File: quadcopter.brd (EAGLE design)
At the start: 178 x 178 mm, 66 parts, among them J1 ISP, SW1 PUSHBUTTON_SMD-VERTICAL-1, U2 ATMEGA128RFA1

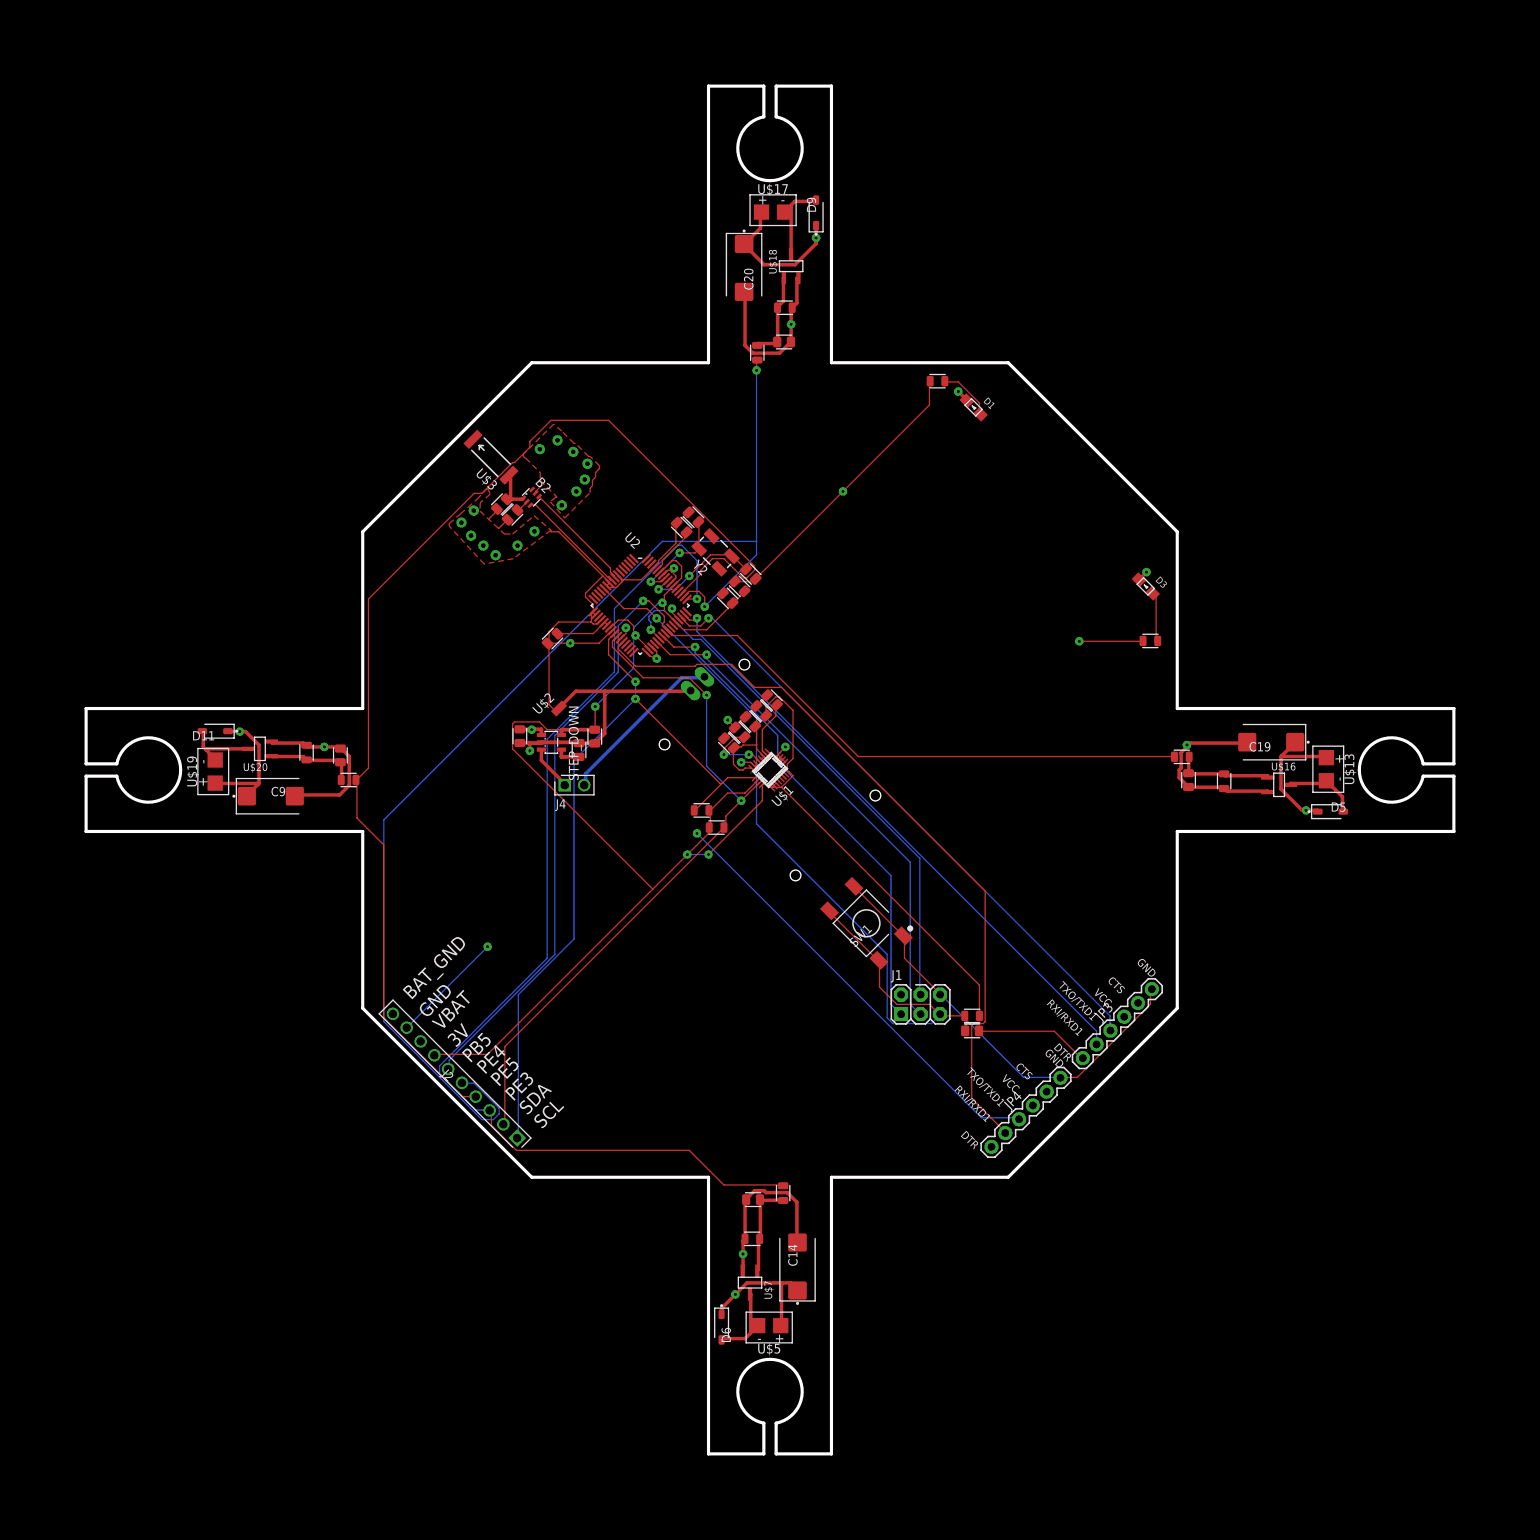
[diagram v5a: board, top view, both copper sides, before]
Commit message: bigger mosfet pads, no vias leading to oscillator, cap 28 and 13 (?) go to gnd instead of bat_gnd, made antenna better
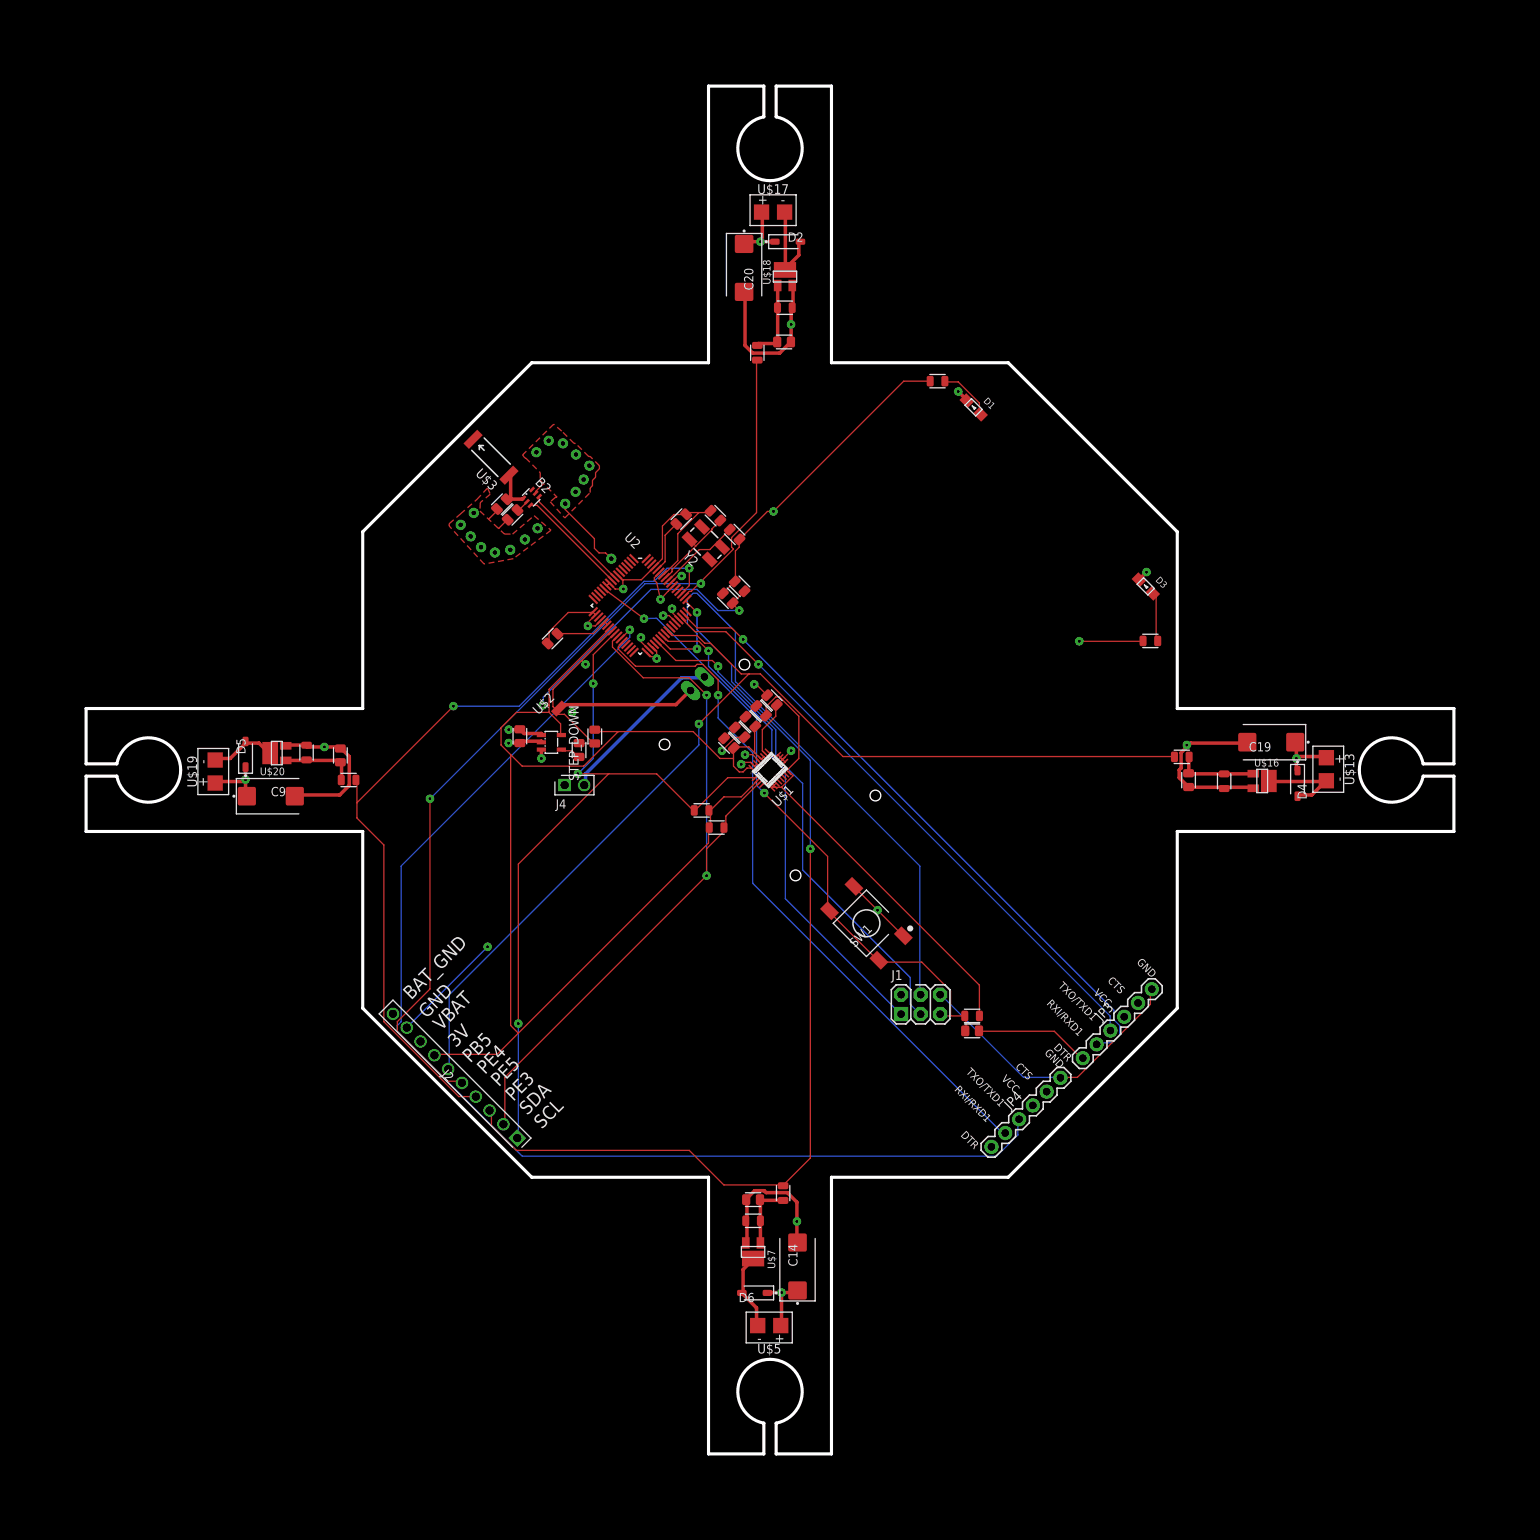
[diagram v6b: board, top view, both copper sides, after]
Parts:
- removed D11, D9: 20V-500MA, quadparts_prebuilt:SOD3716X135_HS
- added D2, D4: (no value), quadparts_prebuilt:SOD3716X135_HS
- D5, D6: value 20V-500MA -> (none)
- moved D5 141.4 mm to (-68.2, 2.05), turned to 90 degrees
- moved D6 6.19 mm to (-2.00, -68.0), turned to 180 degrees
- moved C1 5.56 mm to (-4.60, 30.6)
- moved U$7 4.02 mm to (-2.20, -62.7)
- moved C2 2.86 mm to (-7.10, 33.1)
- moved R10 2.35 mm to (-2.20, -58.7)
- moved U$20 2.27 mm to (-64.2, 2.20)
- moved U$16 2.26 mm to (64.0, -1.43)
- moved Y2 1.73 mm to (-8.34, 29.5)
- moved U$18 1.57 mm to (1.95, 64.2)
- moved C6 1.10 mm to (-11.6, 32.6), turned to 45 degrees
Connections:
- net BAT_GND: no longer C13.2, C28.2
- net FLYBACK: now also D4.A; no longer D5.A
- net FLYBACK1: now also D2.A; no longer D9.A
- net FLYBACK5: now also D5.A; no longer D11.A
- net GND: now also C13.2, C28.2
- net VBAT: now also D2.C, D4.C; no longer D11.C, D9.C
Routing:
- net RX1: track 89.7 -> 157.3 mm, vias 2 -> 1
- net VBAT: track 87.4 -> 41.0 mm, vias 7 -> 8
- net PE5: track 154.8 -> 108.9 mm, vias 0 -> 2
- net 3V: track 244.3 -> 287.6 mm
- net PE4: track 156.7 -> 125.4 mm
- net RESET: track 108.1 -> 84.6 mm, vias 1 -> 2
- net BAT_GND: track 128.8 -> 113.1 mm, vias 5 -> 6
- net PE3: track 143.0 -> 127.8 mm, vias 1 -> 2
- net PB5: track 150.1 -> 140.4 mm
- net MOSI: track 70.2 -> 78.2 mm
- net SDA: track 90.6 -> 98.5 mm
- net TX1: track 97.0 -> 90.8 mm, vias 0 -> 1
- net GND: track 216.0 -> 221.8 mm, vias 24 -> 30
- net TXD1: track 79.1 -> 84.3 mm
- net N$4: track 15.8 -> 11.7 mm, vias 2 -> 0
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
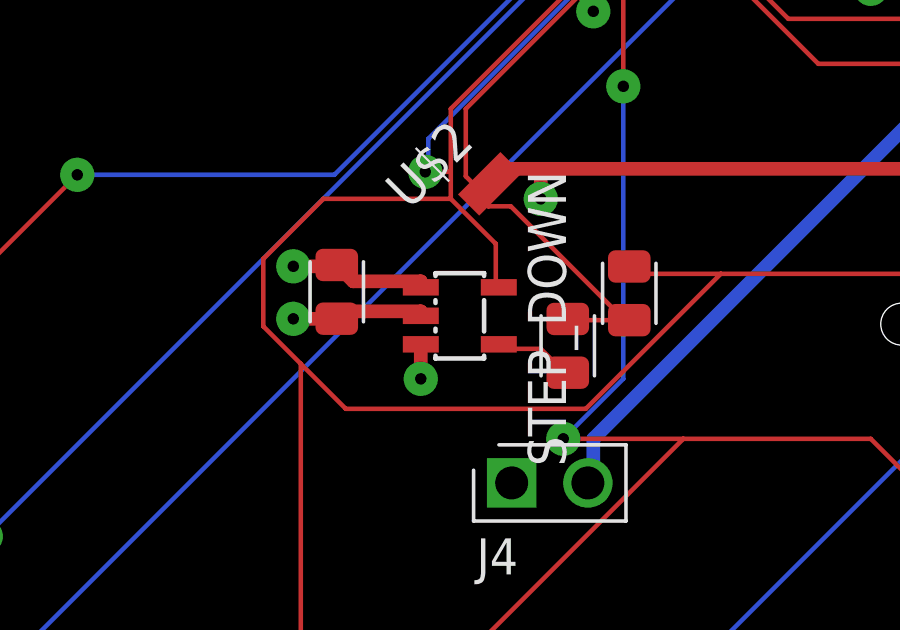
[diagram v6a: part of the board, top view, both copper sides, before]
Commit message: changed most gnds on regulator to gnd instead of bat_gnd
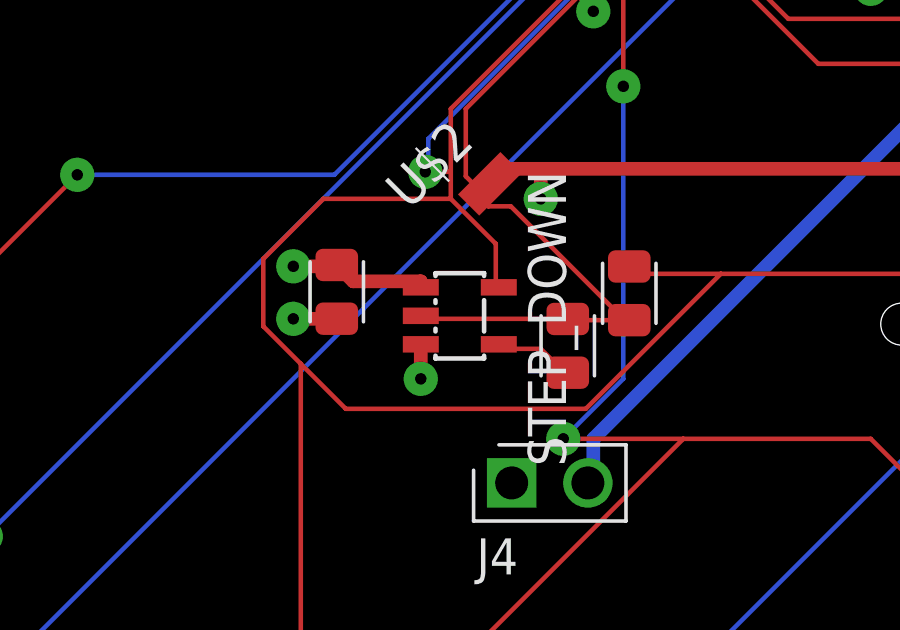
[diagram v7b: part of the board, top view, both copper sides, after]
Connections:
- net BAT_GND: no longer STEP_DOWN.2
- net GND: now also STEP_DOWN.2
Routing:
- net GND: track 221.8 -> 226.8 mm
- net BAT_GND: track 113.1 -> 109.9 mm
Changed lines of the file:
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@@
 <wire x1="-24.85" y1="3.495" x2="-24.81" y2="3.455" width="0.1524" layer="1"/>
 <wire x1="-24.81" y1="3.455" x2="-22.8" y2="3.455" width="0.1524" layer="1"/>
+<contactref element="STEP_DOWN" pad="2"/>
+<wire x1="-25" y1="3.5" x2="-29.75" y2="3.5" width="0.1524" layer="1"/>
+<wire x1="-29.75" y1="3.5" x2="-29.75" y2="3.6" width="0.1524" layer="1"/>
+<wire x1="-25" y1="3.5" x2="-24.85" y2="3.495" width="0.1524" layer="1"/>
 </signal>
 <signal name="N$3">
@@
 <contactref element="C10" pad="2"/>
 <contactref element="U$7" pad="P$2"/>
-<contactref element="STEP_DOWN" pad="2"/>
 <wire x1="3" y1="63" x2="3" y2="60.25" width="0.4572" layer="1"/>
 <wire x1="3" y1="60.25" x2="2.885" y2="60.16" width="0.4572" layer="1"/>
@@
 <via x="2.75" y="58" extent="1-16" drill="0.381"/>
 <via x="-34" y="3.5" extent="1-16" drill="0.381"/>
-<wire x1="-32.5" y1="3.75" x2="-29.75" y2="3.75" width="0.4572" layer="1"/>
-<wire x1="-29.75" y1="3.75" x2="-29.75" y2="3.6" width="0.4572" layer="1"/>
-<wire x1="-32.5" y1="3.75" x2="-32.55" y2="3.505" width="0.4572" layer="1"/>
 <wire x1="-12.25" y1="8.5" x2="-25.75" y2="8.5" width="0.4572" layer="1"/>
 <wire x1="-25.75" y1="8.5" x2="-27" y2="8.5" width="0.4572" layer="1"/>

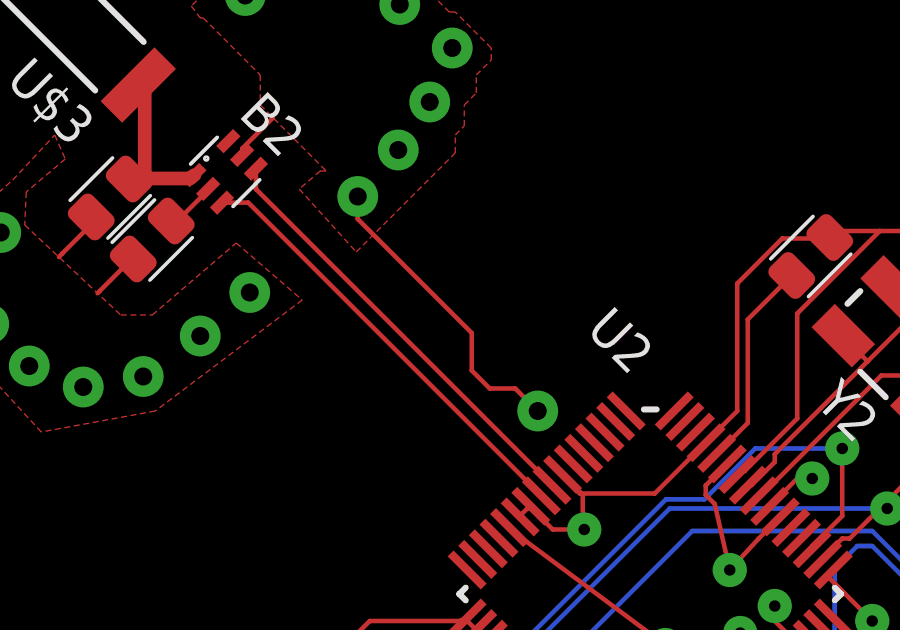
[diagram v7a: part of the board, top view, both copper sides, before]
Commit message: i think i forgot some airwires in last commit
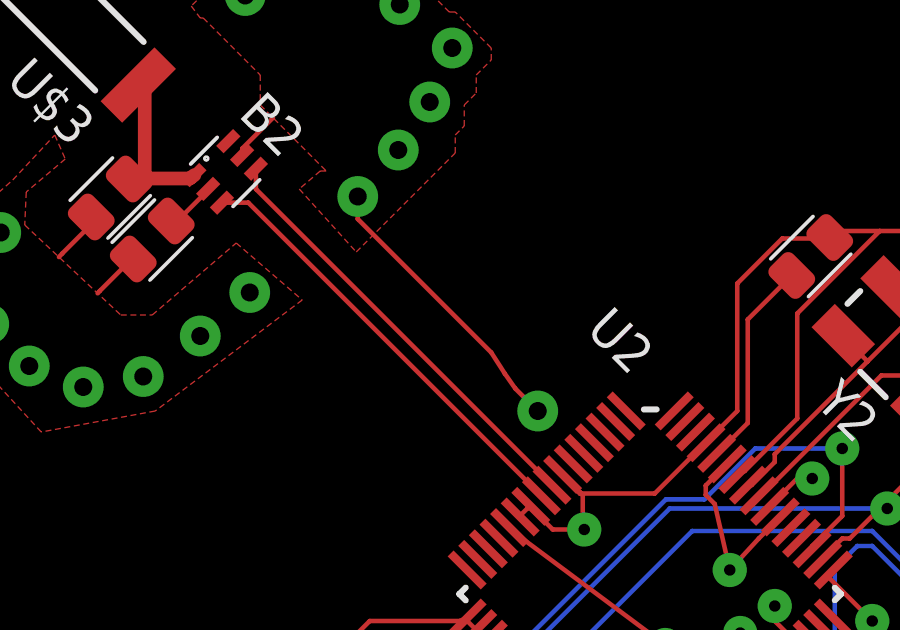
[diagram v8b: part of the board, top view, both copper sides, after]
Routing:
- net GND: track 226.8 -> 226.0 mm
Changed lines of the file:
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@@
 <text x="50.4" y="-26.4" size="1.016" layer="21" font="vector" rot="R135">GND</text>
 <wire x1="-48" y1="35.2" x2="-38.1" y2="24.8" width="0.4064" layer="39"/>
-<wire x1="-38.1" y1="24.8" x2="-31.7" y2="22.6" width="0.4064" layer="39"/>
-<wire x1="-31.7" y1="22.6" x2="-24.4" y2="26.15" width="0.4064" layer="39"/>
-<wire x1="-22.05" y1="29.1" x2="-16" y2="35.05" width="0.4064" layer="39"/>
-<wire x1="-16" y1="35.05" x2="-18.3" y2="40" width="0.4064" layer="39"/>
+<wire x1="-38.1" y1="24.8" x2="-29" y2="21.5" width="0.4064" layer="39"/>
+<wire x1="-29" y1="21.5" x2="-22.15" y2="25.8" width="0.4064" layer="39"/>
+<wire x1="-19.55" y1="28.25" x2="-14.65" y2="33.25" width="0.4064" layer="39"/>
+<wire x1="-14.65" y1="33.25" x2="-18.3" y2="40" width="0.4064" layer="39"/>
 <wire x1="-18.3" y1="40" x2="-30.6" y2="52.4" width="0.4064" layer="39"/>
 <wire x1="-30.6" y1="52.4" x2="-18.3" y2="40.1" width="0.4064" layer="40"/>
-<wire x1="-18.3" y1="40.1" x2="-16.05" y2="35.05" width="0.4064" layer="40"/>
-<wire x1="-16.05" y1="35.05" x2="-22.1" y2="29" width="0.4064" layer="40"/>
-<wire x1="-24.45" y1="26.2" x2="-31.95" y2="22.5" width="0.4064" layer="40"/>
-<wire x1="-31.95" y1="22.5" x2="-38.1" y2="24.8" width="0.4064" layer="40"/>
+<wire x1="-18.3" y1="40.1" x2="-14.65" y2="33.2" width="0.4064" layer="40"/>
+<wire x1="-14.65" y1="33.2" x2="-19.6" y2="28.35" width="0.4064" layer="40"/>
+<wire x1="-22.15" y1="25.8" x2="-28.95" y2="21.45" width="0.4064" layer="40"/>
+<wire x1="-28.95" y1="21.45" x2="-38.1" y2="24.8" width="0.4064" layer="40"/>
 <wire x1="-38.1" y1="24.8" x2="-48" y2="35.2" width="0.4064" layer="40"/>
 </plain>
@@
 <vertex x="-14.89" y="-7.55"/>
 <vertex x="-30.71" y="16.52"/>
-<vertex x="-32.96" y="19.74"/>
-<vertex x="-25.64" y="24"/>
-<vertex x="-23.34" y="25.5"/>
-<vertex x="-16.4" y="32.1"/>
-<vertex x="-11.5" y="37.3"/>
-<vertex x="-6.55" y="43.516"/>
-<vertex x="-5.63" y="43.246"/>
-<vertex x="-4.46" y="43.43"/>
+<vertex x="-31.26" y="16.79"/>
+<vertex x="-26.39" y="20.1"/>
+<vertex x="-21.09" y="25.65"/>
+<vertex x="-22.15" y="27.55"/>
+<vertex x="-20.45" y="29.1"/>
+<vertex x="-18.3" y="27.166"/>
+<vertex x="-7.23" y="38.296"/>
+<vertex x="-2.21" y="43.03"/>
 <vertex x="17.51" y="40.45"/>
 <vertex x="40.14" y="17.55"/>
@@
 <via x="-20.65" y="27.5" extent="1-16" drill="0.6"/>
 <wire x1="-20.65" y1="27.5" x2="-21.4" y2="28.25" width="0.1524" layer="1"/>
-<wire x1="-21.4" y1="28.25" x2="-22.25" y2="28.25" width="0.1524" layer="1"/>
-<wire x1="-22.25" y1="28.25" x2="-22.85" y2="28.85" width="0.1524" layer="1"/>
-<wire x1="-22.85" y1="28.85" x2="-22.85" y2="30.1" width="0.1524" layer="1"/>
-<wire x1="-22.85" y1="30.1" x2="-26.65" y2="33.9" width="0.1524" layer="1"/>
+<wire x1="-21.4" y1="28.25" x2="-21.75" y2="28.75" width="0.1524" layer="1"/>
+<wire x1="-21.75" y1="28.75" x2="-22.2" y2="29.45" width="0.1524" layer="1"/>
+<wire x1="-22.2" y1="29.45" x2="-26.65" y2="33.9" width="0.1524" layer="1"/>
 <wire x1="-26.65" y1="33.9" x2="-26.65" y2="34.65" width="0.1524" layer="1"/>
 <wire x1="-28.75" y1="18" x2="-28.75" y2="16.5" width="0.1524" layer="1"/>
@@
 <wire x1="-28.75" y1="16.5" x2="-28.932859375" y2="16.4671375" width="0.1524" layer="1"/>
 <wire x1="-23.25" y1="20.5" x2="-23.0030375" y2="20.600259375" width="0.1524" layer="1"/>
-<wire x1="-20.5" y1="27.5" x2="-20.65" y2="27.5" width="0.1524" layer="1"/>
 <via x="-19.1" y="23.55" extent="1-16" drill="0.381"/>
 <via x="-23.7" y="18.75" extent="1-16" drill="0.381"/>
@@
 <vertex x="18.8" y="39.2"/>
 <vertex x="17.5" y="40.5"/>
-<vertex x="-6.49" y="43.73"/>
-<vertex x="-23.54" y="25.43"/>
-<vertex x="-27.84" y="23.13"/>
-<vertex x="-33.02" y="19.7"/>
+<vertex x="-1.89" y="42.88"/>
+<vertex x="-5.75" y="39.6"/>
+<vertex x="-17.75" y="27.6"/>
+<vertex x="-17.75" y="26.35"/>
+<vertex x="-20.4" y="29"/>
+<vertex x="-20.6" y="29"/>
+<vertex x="-22.1" y="27.5"/>
+<vertex x="-22.1" y="27.45"/>
+<vertex x="-20.9" y="26.25"/>
+<vertex x="-20.9" y="26.05"/>
+<vertex x="-21.99" y="24.96"/>
+<vertex x="-21.99" y="24.68"/>
+<vertex x="-26.34" y="20.08"/>
+<vertex x="-31.02" y="16.8"/>
 </polygon>
 <contactref element="C3" pad="1"/>
@@
 <vertex x="-48" y="35.3"/>
 <vertex x="-37.9" y="24.8"/>
-<vertex x="-31.8" y="22.7"/>
-<vertex x="-16.05" y="34.95"/>
+<vertex x="-29.65" y="21.8"/>
+<vertex x="-13.9" y="34.05"/>
 <vertex x="-18.3" y="40"/>
 <vertex x="-30.7" y="52.4"/>
@@
 <vertex x="-48" y="35.3"/>
 <vertex x="-37.9" y="24.8"/>
-<vertex x="-32.05" y="22.65"/>
-<vertex x="-16.1" y="35"/>
+<vertex x="-29.85" y="21.65"/>
+<vertex x="-13.9" y="34"/>
 <vertex x="-18.3" y="40"/>
 <vertex x="-30.7" y="52.4"/>
